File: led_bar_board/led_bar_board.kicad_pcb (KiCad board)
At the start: 2 copper layers, 22.7 x 1.8 mm, 15 parts, among them P1 Conn_01x01_Pin, P2 Conn_01x01_Pin, P3 Conn_01x01_Pin

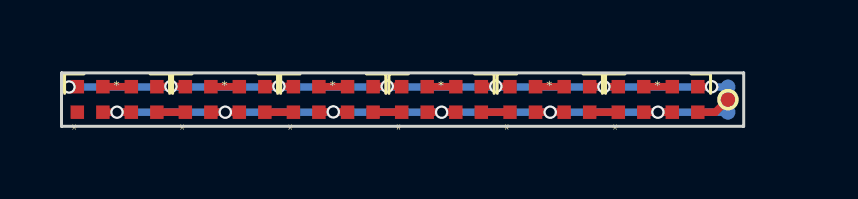
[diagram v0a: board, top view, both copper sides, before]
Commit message: feat(led_bar): modify shape and pad
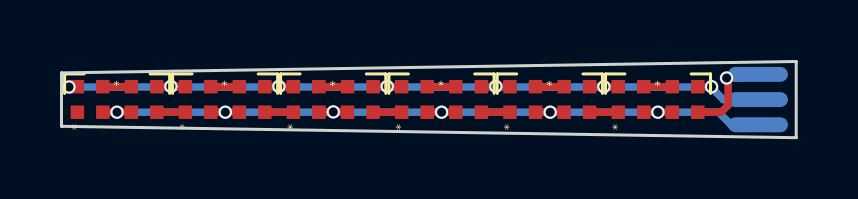
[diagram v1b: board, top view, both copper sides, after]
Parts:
- P2: moved to B.Cu
- moved P2 1.31 mm to (135.6, 103.2), turned to 180 degrees
- moved P1 1.08 mm to (135.6, 104.0)
- moved P3 1.08 mm to (135.6, 104.8)
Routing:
- net /S: track 1.18 -> 2.63 mm, vias 0 -> 1
- net GND: track 26.1 -> 26.7 mm
- net +3.3V: track 27.5 -> 28.1 mm
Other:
- board size 22.7 x 1.8 mm -> 24.5 x 2.5 mm
- board text added: "+"
- board text added: "-"
- board text added: "S"
